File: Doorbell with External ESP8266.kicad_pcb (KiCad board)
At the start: 4 copper layers, 70 x 50 mm, 31 parts, among them J101 Transformer, J102 From Rectifier, J103 To Rectifier, J104 Chime, J105 Button, K101 Relay, Q101 Q_NMOS_GSD, U101 WeMos_D1_mini, U102 XC6220B331MR-G, U103 EL817

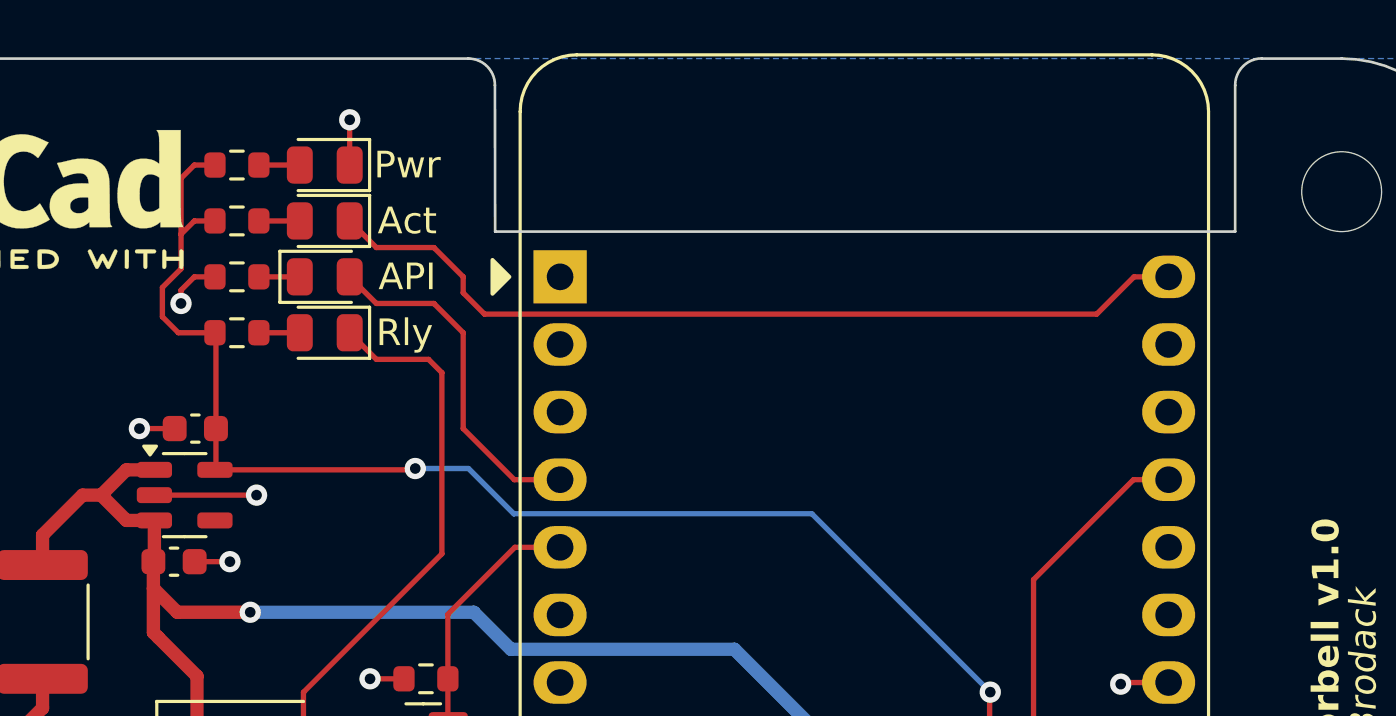
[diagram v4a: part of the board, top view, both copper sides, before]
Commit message: Fix any errors after DRC validation
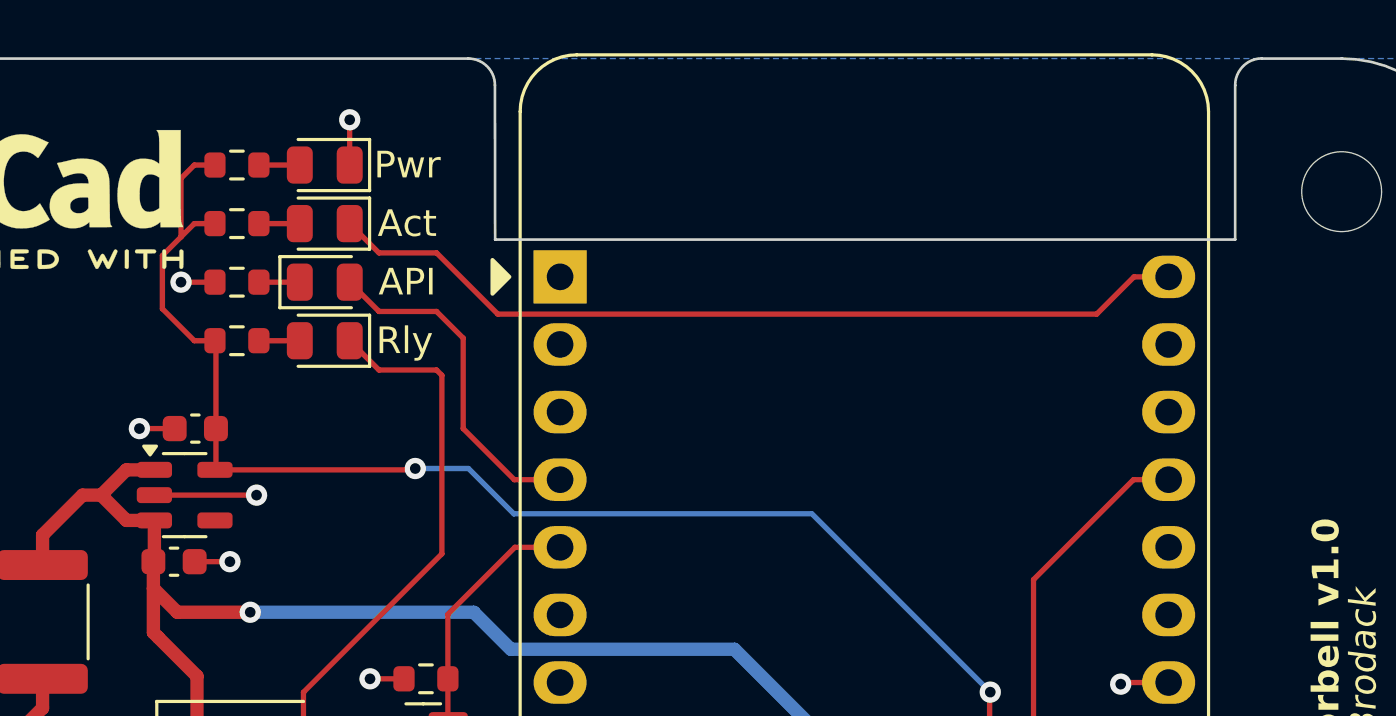
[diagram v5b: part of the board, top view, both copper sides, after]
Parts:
- moved D104 0.30 mm to (46.8, 30.6)
- moved R104 0.30 mm to (43.5, 30.6)
- moved D102 0.20 mm to (46.8, 28.4)
- moved R102 0.20 mm to (43.5, 28.4)
- moved D103 0.10 mm to (46.8, 26.2)
- moved R103 0.10 mm to (43.5, 26.2)
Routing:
- net GND: track 17.3 -> 16.6 mm
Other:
- outline, holes or cut-outs redrawn
